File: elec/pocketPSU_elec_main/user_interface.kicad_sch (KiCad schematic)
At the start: 42 parts, among them J3 Conn_01x12_Pin, Q1 2N7002_C5224215, SW2 EC11J1525402

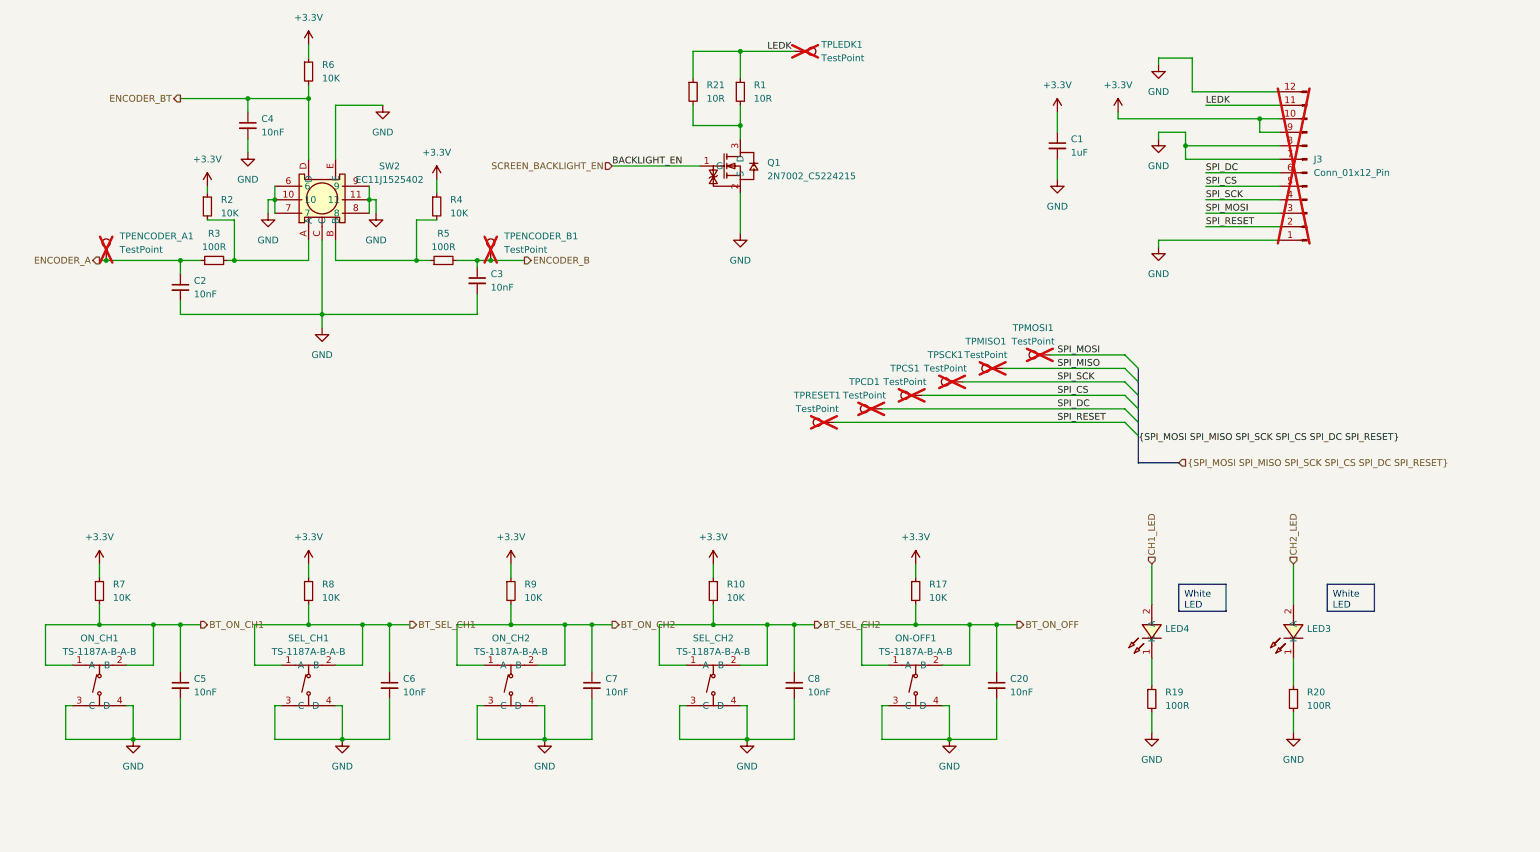
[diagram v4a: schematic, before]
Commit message: make flex pcb for lcd fix
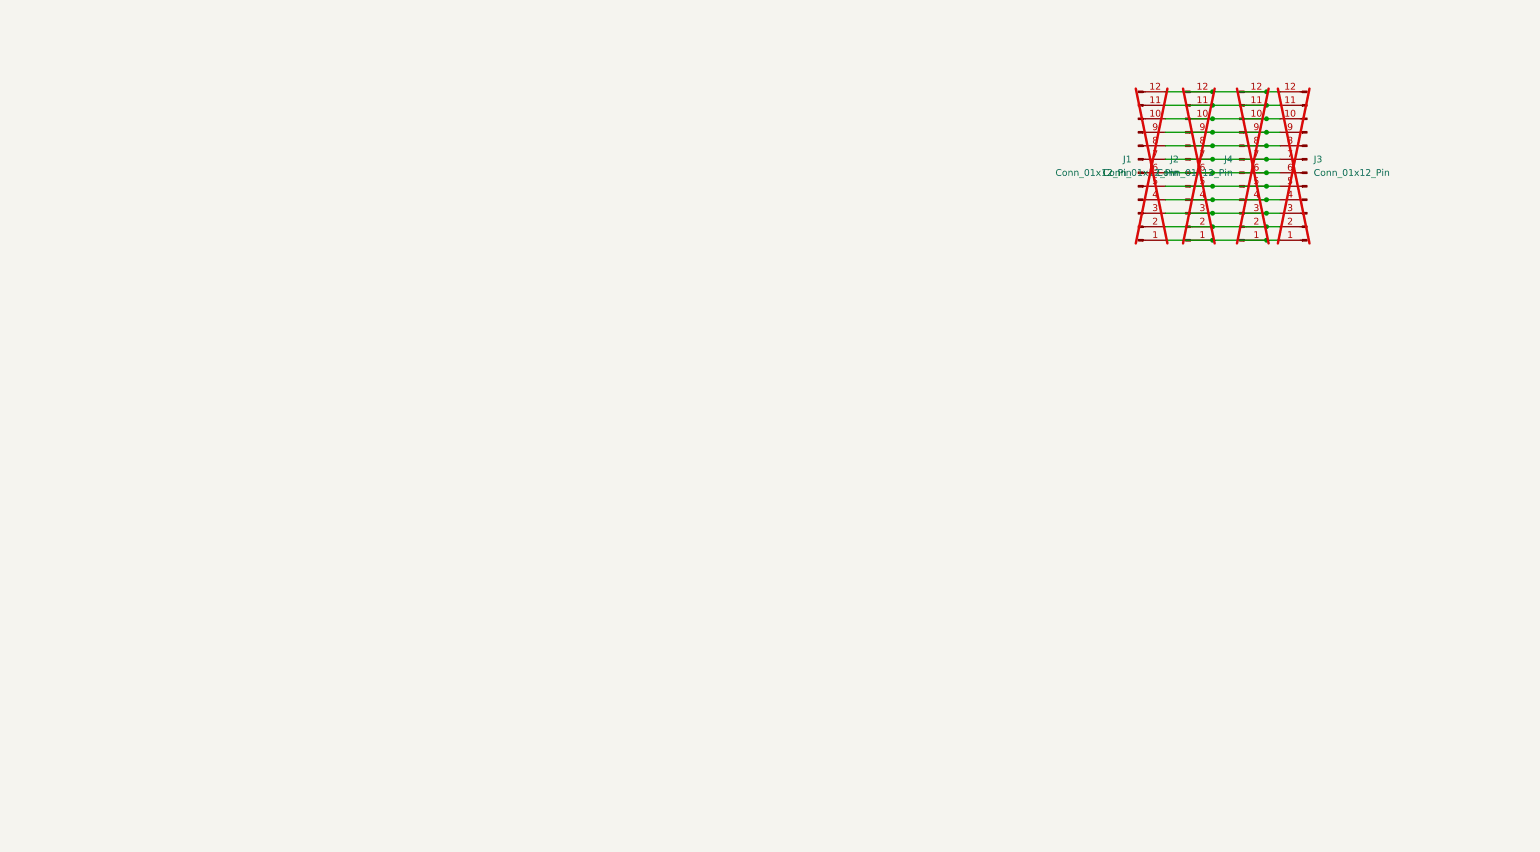
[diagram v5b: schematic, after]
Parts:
- removed C1: 1uF, Resistor_SMD:R_0805_2012Metric, symbol Device:C_Small
- removed C2, C20, C3, C4, C5, C6, C7, C8: 10nF, Capacitor_SMD:C_0402_1005Metric, symbol Device:C_Small
- removed LED3, LED4: F.0603.00026/P2-0603B1TS2-06T-001, footprints:LED0603-RD, symbol footprints:F.0603.00026_P2-0603B1TS2-06T-001
- removed ON-OFF1, ON_CH1, ON_CH2, SEL_CH1, SEL_CH2: TS-1187A-B-A-B, footprints:SW-SMD_4P-L5.1-W5.1-P3.70-LS6.5-TL-2, symbol footprints:TS-1187A-B-A-B
- removed Q1: 2N7002_C5224215, footprints:SOT-23-3_L3.0-W1.6-P1.90-LS2.8-BR, symbol footprints:2N7002_C5224215
- removed R1, R21: 10R, Resistor_SMD:R_0402_1005Metric, symbol Device:R_Small
- removed R10, R17, R2, R4, R6, R7, R8, R9: 10K, Resistor_SMD:R_0402_1005Metric, symbol Device:R_Small
- removed R19, R20, R3, R5: 100R, Resistor_SMD:R_0402_1005Metric, symbol Device:R_Small
- removed SW2: EC11J1525402, footprints:SW-SMD_EC11J1525402, symbol footprints:EC11J1525402
- removed TPCD1, TPCS1, TPENCODER_A1, TPENCODER_B1, TPLEDK1, TPMISO1, TPMOSI1, TPRESET1, TPSCK1: TestPoint, TestPoint:TestPoint_Pad_D1.5mm, symbol Connector:TestPoint
- added J1, J2, J4: Conn_01x12_Pin, footprints:LCD-GMT020-02, symbol Connector:Conn_01x12_Pin
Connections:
- net +3.3V: no longer names the net of J3.10 (Pin_10)
- net +3.3V: now also J1.10 (Pin_10), J2.10 (Pin_10), J4.10 (Pin_10); no longer J3.9 (Pin_9)
- removed net GND: J3.1 (Pin_1), J3.12 (Pin_12), J3.7 (Pin_7), J3.8 (Pin_8)
- net LEDK: no longer names the net of J3.11 (Pin_11)
- net LEDK: now also J1.11 (Pin_11), J2.11 (Pin_11), J4.11 (Pin_11)
- net SPI_CS: no longer names the net of J3.5 (Pin_5)
- net SPI_CS: now also J1.5 (Pin_5), J2.5 (Pin_5), J4.5 (Pin_5)
- net SPI_DC: no longer names the net of J3.6 (Pin_6)
- net SPI_DC: now also J1.6 (Pin_6), J2.6 (Pin_6), J4.6 (Pin_6)
- net SPI_MOSI: no longer names the net of J3.3 (Pin_3)
- net SPI_MOSI: now also J1.3 (Pin_3), J2.3 (Pin_3), J4.3 (Pin_3)
- net SPI_RESET: no longer names the net of J3.2 (Pin_2)
- net SPI_RESET: now also J1.2 (Pin_2), J2.2 (Pin_2), J4.2 (Pin_2)
- net SPI_SCK: no longer names the net of J3.4 (Pin_4)
- net SPI_SCK: now also J1.4 (Pin_4), J2.4 (Pin_4), J4.4 (Pin_4)
- new net: J1.1 (Pin_1), J2.1 (Pin_1), J3.1 (Pin_1), J4.1 (Pin_1)
- new net: J1.12 (Pin_12), J2.12 (Pin_12), J3.12 (Pin_12), J4.12 (Pin_12)
- new net: J1.7 (Pin_7), J2.7 (Pin_7), J3.7 (Pin_7), J4.7 (Pin_7)
- new net: J1.8 (Pin_8), J2.8 (Pin_8), J3.8 (Pin_8), J4.8 (Pin_8)
- new net: J1.9 (Pin_9), J2.9 (Pin_9), J3.9 (Pin_9), J4.9 (Pin_9)
